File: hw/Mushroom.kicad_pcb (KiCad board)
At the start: 2 copper layers, 30 x 30 mm, 28 parts, among them J1 USB_C_Receptacle_PowerOnly_6P, J2 Conn_01x03, J3 Conn_01x12, J4 Conn_01x04, U1 STM32G030F6Px, U2 LPS22HH, U3 SHT30-DIS, U4 BH1750FVI-TR, U5 SPX3819M5-L-3-3

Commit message: Preliminary layout & routing
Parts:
- removed RN2, RN3: 1M, Resistor_SMD:R_Array_Convex_4x0402
- added C10: 100n, Capacitor_SMD:C_0402_1005Metric, F.Cu at (83.5, 43.2)
- added C8: 1u, Capacitor_SMD:C_0402_1005Metric, F.Cu at (83.5, 42.2)
- added C9: 100n, Capacitor_SMD:C_0402_1005Metric, F.Cu at (80.8, 39.3)
- added U6: CH343P, Package_DFN_QFN:QFN-16-1EP_3x3mm_P0.5mm_EP1.9x1.9mm, F.Cu at (80.5, 42.3)
- J1: value USB_C_Receptacle_PowerOnly_6P -> USB_C_Receptacle_USB2.0_14P; footprint Mushroom_footprints:USB_C_Receptacle -> Connector_USB:USB_C_Receptacle_HRO_TYPE-C-31-M-12
- J3: value Conn_01x12 -> Conn_01x04; footprint Mushroom_footprints:Arc_Pins_12 -> Mushroom_footprints:Arc_Pins_04
- moved C3 18.4 mm to (76.4, 55.8), turned to 0 degrees
- moved U3 14.9 mm to (76.5, 53.6), turned to -90 degrees
- moved C2 14.5 mm to (79.8, 55.4), turned to 180 degrees
- moved R3 13.9 mm to (83.9, 55.0), turned to 180 degrees
- moved R1 13.7 mm to (75.2, 51.4), turned to 0 degrees
- moved C5 13.2 mm to (82.1, 55.0), turned to 180 degrees
- moved C4 12.6 mm to (85.4, 53.6), turned to 90 degrees
- moved U2 11.4 mm to (79.6, 53.7), turned to 180 degrees
- moved U4 10.6 mm to (83.1, 53.6), turned to 180 degrees
- moved R2 8.96 mm to (84.8, 51.3), turned to 180 degrees
- moved C1 6.01 mm to (84.3, 49.1), turned to 90 degrees
- moved RN1 3.54 mm to (75.2, 48.3)
- moved U1 2.73 mm to (80.0, 48.3), turned to 180 degrees
- moved R5 1.28 mm to (82.0, 39.3), turned to -90 degrees
- moved R4 1.20 mm to (78.1, 39.3), turned to -90 degrees
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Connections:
- J1 pad A5: Net-(J1-CC1) -> /CC1
- J1 pad B5: Net-(J1-CC2) -> /CC2
- R4 pad 1: Net-(J1-CC2) -> /CC2
- R5 pad 1: Net-(J1-CC1) -> /CC1
- U1 pad 10: /TOUCH_3 -> /UART_RX
- U1 pad 11: /TOUCH_4 -> /CC2
- U1 pad 12: /TOUCH_5 -> /LED_OUT
- U1 pad 13: /TOUCH_6 -> /TOUCH_OUT
- U1 pad 14: /TOUCH_7 -> /TOUCH_0
- U1 pad 15: /TOUCH_8 -> /TOUCH_1
- U1 pad 16: /TOUCH_9 -> /TOUCH_2
- U1 pad 17: /TOUCH_10 -> /TOUCH_3
- U1 pad 2: /LED_OUT -> unconnected-(U1-PC14/PB9-Pad2)
- U1 pad 3: /TOUCH_OUT -> unconnected-(U1-PC15-Pad3)
- U1 pad 7: /TOUCH_0 -> unconnected-(U1-PA0-Pad7)
- U1 pad 8: /TOUCH_1 -> /CC1
- U1 pad 9: /TOUCH_2 -> /UART_TX
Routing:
- net /CC2: track 0.00 -> 17.9 mm, vias 0 -> 2
- net /TOUCH_OUT: track 21.8 -> 4.38 mm, vias 5 -> 2
- net /TOUCH_6: track 16.9 -> 0.00 mm
- net +3V3: track 35.1 -> 51.5 mm
- net /TOUCH_7: track 15.3 -> 0.00 mm
- net /TOUCH_4: track 14.7 -> 0.00 mm
- net /TOUCH_5: track 14.4 -> 0.00 mm
- net /CC1: track 0.00 -> 13.9 mm
- net /TOUCH_8: track 12.8 -> 0.00 mm
- net /TOUCH_10: track 11.6 -> 0.00 mm
- net /TOUCH_9: track 11.5 -> 0.00 mm
- net /SWCLK: track 7.52 -> 18.7 mm, vias 0 -> 2
- net /UART_TX: track 0.00 -> 9.00 mm, vias 0 -> 2
- net /UART_RX: track 0.00 -> 8.64 mm
- net /USB_D-: track 0.00 -> 8.11 mm, vias 0 -> 2
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- removed copper zone on F.Cu, net +3V3

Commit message: 🎉 Finalise design; submit for fab (Rev. 2)
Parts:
- moved C2 1.50 mm to (81.3, 55.4)
- moved C3 1.50 mm to (77.9, 55.8)
- moved C4 1.50 mm to (86.9, 53.6)
- moved C5 1.50 mm to (83.6, 55.0)
- moved R3 1.50 mm to (85.4, 55.0)
- moved U2 1.50 mm to (81.1, 53.7)
- moved U3 1.50 mm to (78.0, 53.6)
- moved U4 1.50 mm to (84.6, 53.6)
- moved R1 0.57 mm to (75.7, 51.8), turned to 90 degrees
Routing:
- net /SCL: track 10.2 -> 11.3 mm
- net +3V3: track 51.5 -> 52.3 mm
- net /USB_D-: track 8.11 -> 7.61 mm
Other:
- board text added: "<24-Frost"
- board text added: "JLCJLCJLCJLC"
- board text added: "Rev. 2"
- board text removed: "<24-Chill"
- board text removed: "Rev. 1"

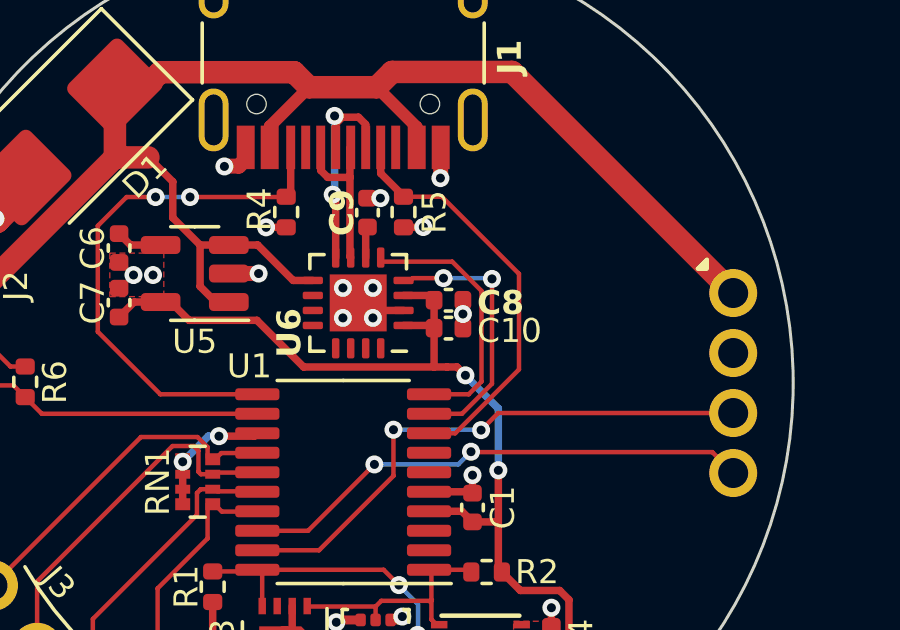
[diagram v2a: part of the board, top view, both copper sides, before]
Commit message: Fix TX/RX lines; re-submit for fab (Rev. 2)
Previous order was cancelled (Y52, Y53)
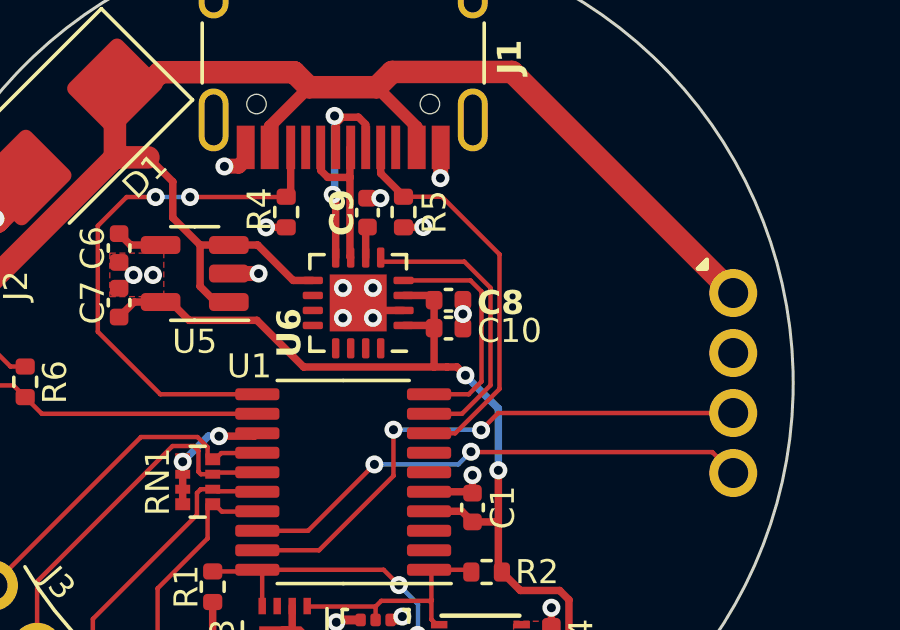
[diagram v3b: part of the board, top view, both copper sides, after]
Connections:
- U6 pad 4: /UART_TX -> /UART_RX
- U6 pad 5: /UART_RX -> /UART_TX
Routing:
- net /UART_RX: track 8.70 -> 7.67 mm
- net /UART_TX: track 9.00 -> 9.70 mm, vias 2 -> 0
- net /CC1: track 13.9 -> 13.4 mm
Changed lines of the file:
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@@
       (net 1 "+3V3") (pinfunction "VDD5") (pintype "passive"))
     (pad "4" smd roundrect (at -1.5125 0.75 180) (size 0.675 0.25) (layers "F.Cu" "F.Paste" "F.Mask") (roundrect_rratio 0.25)
-      (net 18 "/UART_TX") (pinfunction "TXD") (pintype "passive"))
+      (net 28 "/UART_RX") (pinfunction "TXD") (pintype "passive"))
     (pad "5" smd roundrect (at -0.75 1.5125 180) (size 0.25 0.675) (layers "F.Cu" "F.Paste" "F.Mask") (roundrect_rratio 0.25)
-      (net 28 "/UART_RX") (pinfunction "RXD") (pintype "passive"))
+      (net 18 "/UART_TX") (pinfunction "RXD") (pintype "passive"))
     (pad "6" smd roundrect (at -0.25 1.5125 180) (size 0.25 0.675) (layers "F.Cu" "F.Paste" "F.Mask") (roundrect_rratio 0.25)
       (net 6 "Net-(U6-V3)") (pinfunction "V3") (pintype "passive"))
@@
   (segment (start 80.75 40.8175) (end 80.75 39.86) (width 0.25) (layer "F.Cu") (net 6))
   (segment (start 80.75 39.86) (end 80.81 39.8) (width 0.25) (layer "F.Cu") (net 6))
+  (segment (start 83.733527 46.675) (end 82.8625 46.675) (width 0.15) (layer "F.Cu") (net 7))
   (segment (start 82.01 38.77) (end 82.01 38.79) (width 0.25) (layer "F.Cu") (net 7))
-  (segment (start 83.733527 46.675) (end 82.8625 46.675) (width 0.15) (layer "F.Cu") (net 7))
   (segment (start 82.01 38.79) (end 83.29 38.79) (width 0.15) (layer "F.Cu") (net 7))
-  (segment (start 85.86 44.548527) (end 83.733527 46.675) (width 0.15) (layer "F.Cu") (net 7))
   (segment (start 81.25 37.145) (end 81.25 38.01) (width 0.25) (layer "F.Cu") (net 7))
-  (segment (start 83.29 38.79) (end 85.86 41.36) (width 0.15) (layer "F.Cu") (net 7))
-  (segment (start 85.86 41.36) (end 85.86 44.548527) (width 0.15) (layer "F.Cu") (net 7))
+  (segment (start 85.21 45.198527) (end 83.733527 46.675) (width 0.15) (layer "F.Cu") (net 7))
   (segment (start 81.25 38.01) (end 82.01 38.77) (width 0.25) (layer "F.Cu") (net 7))
+  (segment (start 85.21 40.71) (end 85.21 45.198527) (width 0.15) (layer "F.Cu") (net 7))
+  (segment (start 83.29 38.79) (end 85.21 40.71) (width 0.15) (layer "F.Cu") (net 7))
   (segment (start 67 45.08) (end 69.01 45.08) (width 0.15) (layer "F.Cu") (net 9))
   (segment (start 69.4 45.47) (end 69.955 46.025) (width 0.15) (layer "F.Cu") (net 9))
@@
   (segment (start 79.713109 36.096791) (end 79.72 36.103682) (width 0.25) (layer "B.Cu") (net 15))
   (segment (start 79.713109 36.096791) (end 79.713109 38.656891) (width 0.25) (layer "B.Cu") (net 15))
+  (segment (start 73.745 38.8) (end 72.78 38.8) (width 0.15) (layer "F.Cu") (net 16))
   (segment (start 78.25 37.145) (end 78.25 38.64) (width 0.25) (layer "F.Cu") (net 16))
   (segment (start 78.09 38.8) (end 78.1 38.79) (width 0.15) (layer "F.Cu") (net 16))
-  (segment (start 73.745 38.8) (end 72.78 38.8) (width 0.15) (layer "F.Cu") (net 16))
+  (segment (start 72.78 38.8) (end 71.82 39.76) (width 0.15) (layer "F.Cu") (net 16))
   (segment (start 78.25 38.64) (end 78.1 38.79) (width 0.25) (layer "F.Cu") (net 16))
   (segment (start 74.895 38.8) (end 78.09 38.8) (width 0.15) (layer "F.Cu") (net 16))
@@
   (segment (start 71.82 43.29) (end 73.905 45.375) (width 0.15) (layer "F.Cu") (net 16))
   (segment (start 71.82 39.76) (end 71.82 43.29) (width 0.15) (layer "F.Cu") (net 16))
-  (segment (start 72.78 38.8) (end 71.82 39.76) (width 0.15) (layer "F.Cu") (net 16))
   (via (at 73.745 38.8) (size 0.6) (drill 0.3) (layers "F.Cu" "B.Cu") (net 16))
   (via (at 74.895 38.8) (size 0.6) (drill 0.3) (layers "F.Cu" "B.Cu") (net 16))
   (segment (start 74.895 38.8) (end 73.745 38.8) (width 0.15) (layer "B.Cu") (net 16))
-  (segment (start 84.96 41.53) (end 84.96 45.024263) (width 0.15) (layer "F.Cu") (net 18))
-  (segment (start 84.96 45.024263) (end 83.959263 46.025) (width 0.15) (layer "F.Cu") (net 18))
-  (segment (start 82.315228 41.504772) (end 82.24 41.58) (width 0.15) (layer "F.Cu") (net 18))
+  (segment (start 84.91 41.825736) (end 84.91 45.074263) (width 0.15) (layer "F.Cu") (net 18))
+  (segment (start 84.039264 40.955) (end 84.91 41.825736) (width 0.15) (layer "F.Cu") (net 18))
+  (segment (start 81.265 40.955) (end 84.039264 40.955) (width 0.15) (layer "F.Cu") (net 18))
   (segment (start 83.959263 46.025) (end 82.8625 46.025) (width 0.15) (layer "F.Cu") (net 18))
-  (segment (start 82.24 41.58) (end 82.0125 41.58) (width 0.15) (layer "F.Cu") (net 18))
-  (segment (start 83.342377 41.504772) (end 82.315228 41.504772) (width 0.15) (layer "F.Cu") (net 18))
-  (via (at 84.96 41.53) (size 0.6) (drill 0.3) (layers "F.Cu" "B.Cu") (net 18))
-  (via (at 83.342377 41.504772) (size 0.6) (drill 0.3) (layers "F.Cu" "B.Cu") (net 18))
-  (segment (start 84.934772 41.504772) (end 84.96 41.53) (width 0.15) (layer "B.Cu") (net 18))
-  (segment (start 83.342377 41.504772) (end 84.934772 41.504772) (width 0.15) (layer "B.Cu") (net 18))
+  (segment (start 81.26 40.96) (end 81.265 40.955) (width 0.15) (layer "F.Cu") (net 18))
+  (segment (start 84.91 45.074263) (end 83.959263 46.025) (width 0.15) (layer "F.Cu") (net 18))
   (segment (start 84.596232 46.57) (end 85.166232 46) (width 0.15) (layer "F.Cu") (net 19))
   (segment (start 79.195 50.575) (end 77.1375 50.575) (width 0.15) (layer "F.Cu") (net 19))
@@
   (segment (start 75.858455 46.771871) (end 75.503129 46.771871) (width 0.25) (layer "B.Cu") (net 23))
   (segment (start 75.503129 46.771871) (end 74.65 47.625) (width 0.25) (layer "B.Cu") (net 23))
-  (segment (start 84.61 41.93) (end 83.635 40.955) (width 0.15) (layer "F.Cu") (net 28))
-  (segment (start 83.635 40.955) (end 81.265 40.955) (width 0.15) (layer "F.Cu") (net 28))
-  (segment (start 84.184999 45.375) (end 84.61 44.949999) (width 0.15) (layer "F.Cu") (net 28))
-  (segment (start 81.265 40.955) (end 81.26 40.96) (width 0.15) (layer "F.Cu") (net 28))
-  (segment (start 84.61 44.949999) (end 84.61 41.93) (width 0.15) (layer "F.Cu") (net 28))
-  (segment (start 82.8625 45.375) (end 84.184999 45.375) (width 0.15) (layer "F.Cu") (net 28))
+  (segment (start 84.24 41.58) (end 84.61 41.95) (width 0.15) (layer "F.Cu") (net 28))
+  (segment (start 82.0125 41.58) (end 84.24 41.58) (width 0.15) (layer "F.Cu") (net 28))
+  (segment (start 84.61 44.949999) (end 84.184999 45.375) (width 0.15) (layer "F.Cu") (net 28))
+  (segment (start 84.184999 45.375) (end 82.8625 45.375) (width 0.15) (layer "F.Cu") (net 28))
+  (segment (start 84.61 41.95) (end 84.61 44.949999) (width 0.15) (layer "F.Cu") (net 28))
   (segment (start 82.8625 50.575) (end 82.8875 50.6) (width 0.15) (layer "F.Cu") (net 36))
   (zone (net 5) (net_name "+5V") (layer "F.Cu") (hatch edge 0.5)
